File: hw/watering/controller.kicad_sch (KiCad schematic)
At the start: 20 parts, among them SW2 KMS221GLFS, SW3 KMS221GLFS, U1 ESP32-C6, U3 W25Q128JVS, Y1 40MHz, Y2 32768Hz

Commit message: - improved voltage boost on battery power - some issues with rtc clock - some issues with pwm that result in brownout
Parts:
- removed C5, C6, C7: 100n, Capacitor_SMD:C_0603_1608Metric, symbol Device:C
- added C22: 1u, Capacitor_SMD:C_0603_1608Metric, symbol Device:C
- added C37, C38, C39: 22u, Capacitor_SMD:C_1206_3216Metric, symbol Device:C
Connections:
- net +3V3: now also C37.1, C38.1, C39.1
- net GND: now also C22.2, C37.2, C38.2, C39.2
- net at U1.23 (VDD_SPI/GPIO27), U3.8 (VCC): now also C22.1

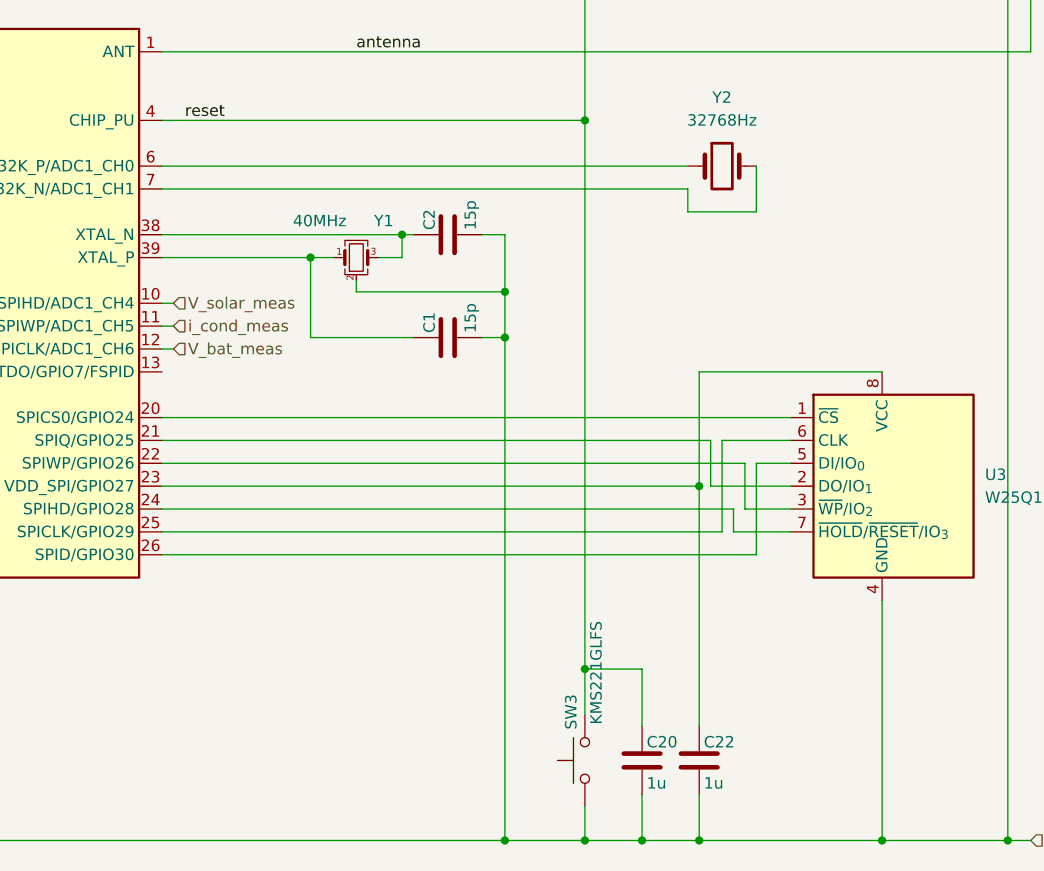
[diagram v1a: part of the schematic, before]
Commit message: - fixed formatting - proper pwm output for conductivity output
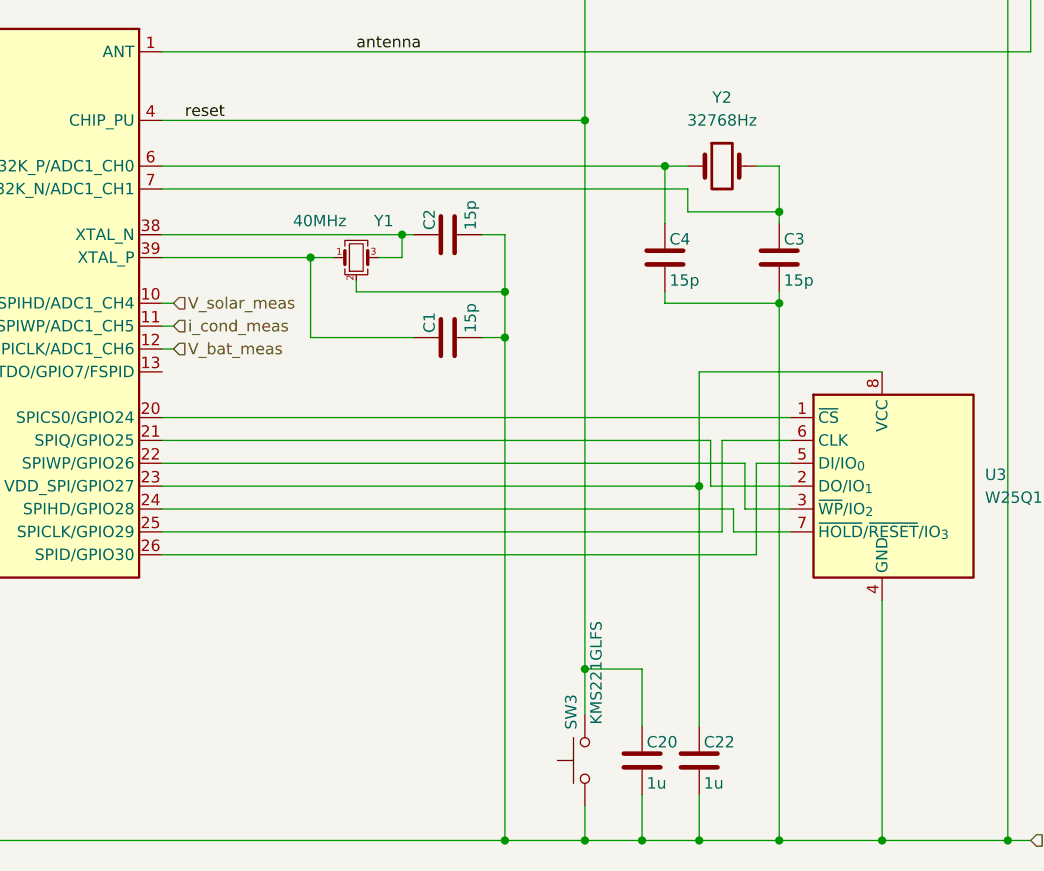
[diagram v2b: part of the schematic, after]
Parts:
- added C3, C4: 15p, Capacitor_SMD:C_0603_1608Metric, symbol Device:C
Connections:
- net GND: now also C3.2, C4.2
- net at U1.6 (GPIO0/XTAL_32K_P/ADC1_CH0), Y2.1: now also C4.1
- net at U1.7 (GPIO1/XTAL_32K_N/ADC1_CH1), Y2.2: now also C3.1
